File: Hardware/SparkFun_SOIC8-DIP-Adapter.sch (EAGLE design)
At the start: 15 parts, among them U1 GENERIC-SOIC8, U2 GENERIC-SOIC8, U3 GENERIC-SOIC8, U4 GENERIC-SOIC8

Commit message: Some small updates
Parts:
- FRAME1: value (none) -> frame
- JP1, JP2, JP3, JP4, JP5, JP6, JP7, JP8: value (none) -> 1x4
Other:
- note added: "Four SOIC8 to DIP adapters on one snappable board."
- note added: "V11"
- note removed: "V01"
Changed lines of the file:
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@@
 </classes>
 <parts>
-<part name="FRAME1" library="SparkFun-Aesthetics" deviceset="FRAME-LETTER" device=""/>
+<part name="FRAME1" library="SparkFun-Aesthetics" deviceset="FRAME-LETTER" device="" value="frame"/>
 <part name="U1" library="SparkFun-AnalogIC" deviceset="GENERIC-SOIC8" device=""/>
 <part name="U2" library="SparkFun-AnalogIC" deviceset="GENERIC-SOIC8" device=""/>
 <part name="U3" library="SparkFun-AnalogIC" deviceset="GENERIC-SOIC8" device=""/>
 <part name="U4" library="SparkFun-AnalogIC" deviceset="GENERIC-SOIC8" device=""/>
-<part name="JP1" library="SparkFun-Connectors" deviceset="M04" device="NO_SILK_ALL_ROUND"/>
-<part name="JP2" library="SparkFun-Connectors" deviceset="M04" device="NO_SILK_ALL_ROUND"/>
-<part name="JP3" library="SparkFun-Connectors" deviceset="M04" device="NO_SILK_ALL_ROUND"/>
-<part name="JP4" library="SparkFun-Connectors" deviceset="M04" device="NO_SILK_ALL_ROUND"/>
-<part name="JP5" library="SparkFun-Connectors" deviceset="M04" device="NO_SILK_ALL_ROUND"/>
-<part name="JP6" library="SparkFun-Connectors" deviceset="M04" device="NO_SILK_ALL_ROUND"/>
-<part name="JP7" library="SparkFun-Connectors" deviceset="M04" device="NO_SILK_ALL_ROUND"/>
-<part name="JP8" library="SparkFun-Connectors" deviceset="M04" device="NO_SILK_ALL_ROUND"/>
+<part name="JP1" library="SparkFun-Connectors" deviceset="M04" device="NO_SILK_ALL_ROUND" value="1x4"/>
+<part name="JP2" library="SparkFun-Connectors" deviceset="M04" device="NO_SILK_ALL_ROUND" value="1x4"/>
+<part name="JP3" library="SparkFun-Connectors" deviceset="M04" device="NO_SILK_ALL_ROUND" value="1x4"/>
+<part name="JP4" library="SparkFun-Connectors" deviceset="M04" device="NO_SILK_ALL_ROUND" value="1x4"/>
+<part name="JP5" library="SparkFun-Connectors" deviceset="M04" device="NO_SILK_ALL_ROUND" value="1x4"/>
+<part name="JP6" library="SparkFun-Connectors" deviceset="M04" device="NO_SILK_ALL_ROUND" value="1x4"/>
+<part name="JP7" library="SparkFun-Connectors" deviceset="M04" device="NO_SILK_ALL_ROUND" value="1x4"/>
+<part name="JP8" library="SparkFun-Connectors" deviceset="M04" device="NO_SILK_ALL_ROUND" value="1x4"/>
 <part name="LOGO1" library="SparkFun-Aesthetics" deviceset="SFE_LOGO_FLAME" device=".1_INCH"/>
 <part name="LOGO2" library="SparkFun-Aesthetics" deviceset="OSHW-LOGO" device="S"/>
@@
 <plain>
 <text x="172.72" y="10.16" size="2.54" layer="94">Byron Jacquot</text>
-<text x="238.76" y="7.62" size="2.54" layer="94">V01</text>
+<text x="238.76" y="7.62" size="2.54" layer="94">V11</text>
+<text x="68.58" y="172.72" size="2.54" layer="94">Four SOIC8 to DIP adapters on one snappable board.</text>
 </plain>
 <instances>

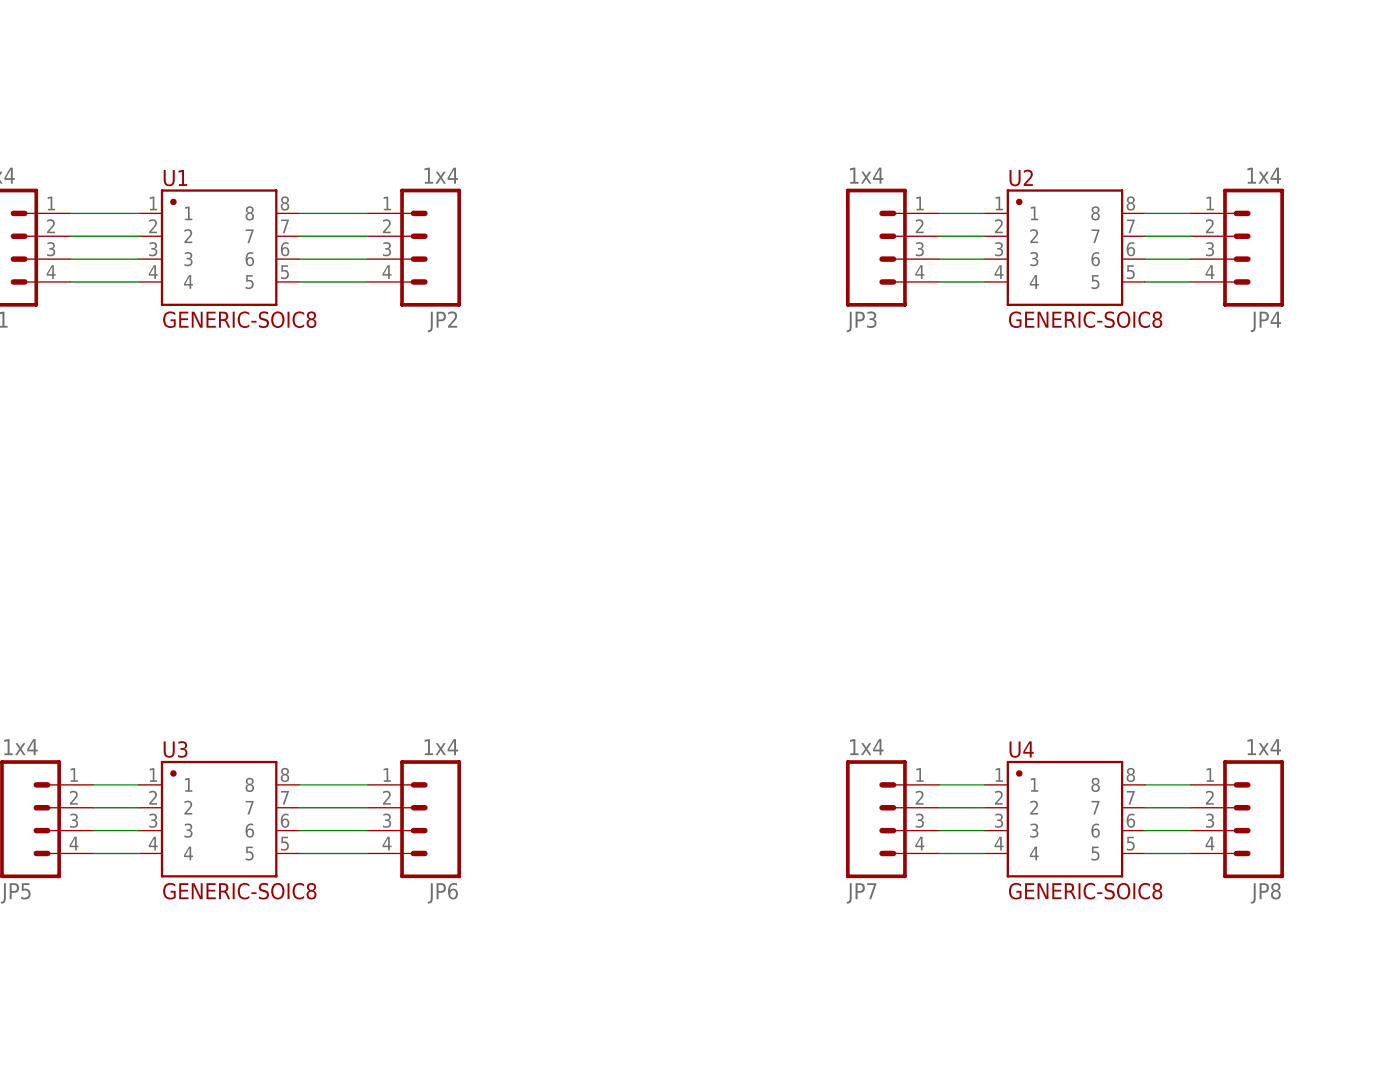
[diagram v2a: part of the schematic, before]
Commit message: Checklist-related updates.
Should handle all issues:
-names/values were on wring layers
-added dimension lines
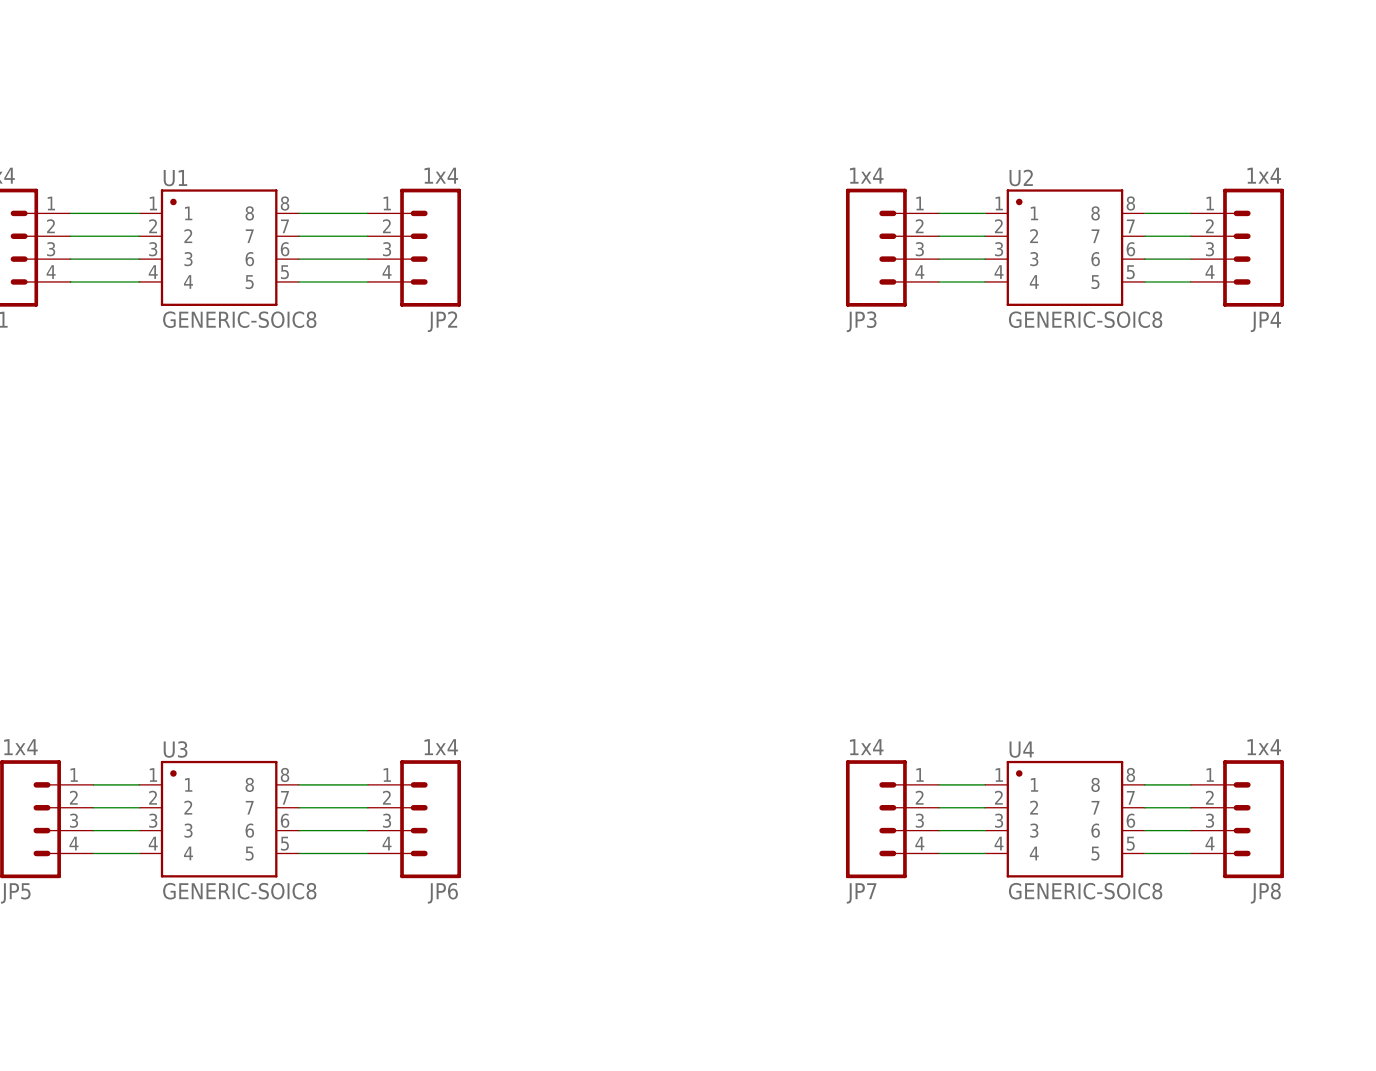
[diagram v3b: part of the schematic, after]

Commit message: Updates after reviewing protos.
Wider SOIC footprint.
DIP pin 1 marked with square pad.
Some rearrangement of silk elements.
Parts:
- JP1, JP3, JP5, JP7: device SparkFun-Connectors:M04NO_SILK_ALL_ROUND -> SparkFun-Connectors:M041X04_NO_SILK
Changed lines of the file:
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@@
 <part name="U3" library="SparkFun-AnalogIC" deviceset="GENERIC-SOIC8" device=""/>
 <part name="U4" library="SparkFun-AnalogIC" deviceset="GENERIC-SOIC8" device=""/>
-<part name="JP1" library="SparkFun-Connectors" deviceset="M04" device="NO_SILK_ALL_ROUND" value="1x4"/>
+<part name="JP1" library="SparkFun-Connectors" deviceset="M04" device="1X04_NO_SILK" value="1x4"/>
 <part name="JP2" library="SparkFun-Connectors" deviceset="M04" device="NO_SILK_ALL_ROUND" value="1x4"/>
-<part name="JP3" library="SparkFun-Connectors" deviceset="M04" device="NO_SILK_ALL_ROUND" value="1x4"/>
+<part name="JP3" library="SparkFun-Connectors" deviceset="M04" device="1X04_NO_SILK" value="1x4"/>
 <part name="JP4" library="SparkFun-Connectors" deviceset="M04" device="NO_SILK_ALL_ROUND" value="1x4"/>
-<part name="JP5" library="SparkFun-Connectors" deviceset="M04" device="NO_SILK_ALL_ROUND" value="1x4"/>
+<part name="JP5" library="SparkFun-Connectors" deviceset="M04" device="1X04_NO_SILK" value="1x4"/>
 <part name="JP6" library="SparkFun-Connectors" deviceset="M04" device="NO_SILK_ALL_ROUND" value="1x4"/>
-<part name="JP7" library="SparkFun-Connectors" deviceset="M04" device="NO_SILK_ALL_ROUND" value="1x4"/>
+<part name="JP7" library="SparkFun-Connectors" deviceset="M04" device="1X04_NO_SILK" value="1x4"/>
 <part name="JP8" library="SparkFun-Connectors" deviceset="M04" device="NO_SILK_ALL_ROUND" value="1x4"/>
 <part name="LOGO1" library="SparkFun-Aesthetics" deviceset="SFE_LOGO_FLAME" device=".1_INCH"/>

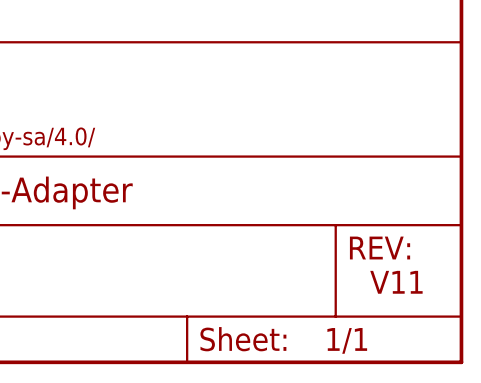
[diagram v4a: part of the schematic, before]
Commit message: Fixing review issues
* CC block location.
* Ver # mismatch between schem and PCB.
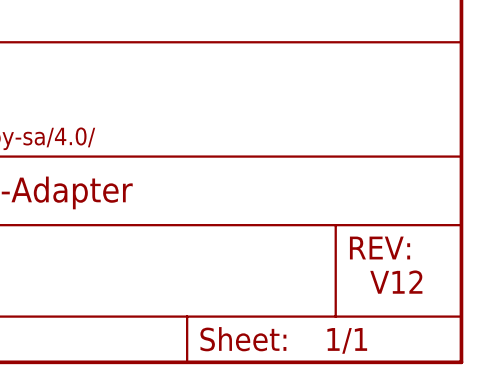
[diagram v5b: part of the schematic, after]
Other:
- note added: "V12"
- note removed: "V11"
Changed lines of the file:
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@@
 <plain>
 <text x="172.72" y="10.16" size="2.54" layer="94">Byron Jacquot</text>
-<text x="238.76" y="7.62" size="2.54" layer="94">V11</text>
+<text x="238.76" y="7.62" size="2.54" layer="94">V12</text>
 <text x="68.58" y="172.72" size="2.54" layer="94">Four SOIC8 to DIP adapters on one snappable board.</text>
 </plain>

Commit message: Moving version numbers back to V11, matching branch name.
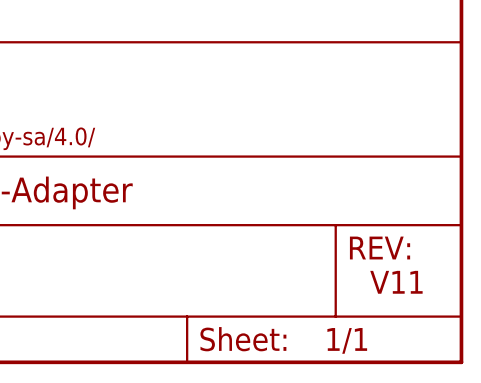
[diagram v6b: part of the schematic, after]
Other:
- note added: "V11"
- note removed: "V12"
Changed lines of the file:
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@@
 <?xml version="1.0" encoding="utf-8"?>
 <!DOCTYPE eagle SYSTEM "eagle.dtd">
-<eagle version="7.1.0">
+<eagle version="7.3.0">
 <drawing>
 <settings>
@@
 <plain>
 <text x="172.72" y="10.16" size="2.54" layer="94">Byron Jacquot</text>
-<text x="238.76" y="7.62" size="2.54" layer="94">V12</text>
+<text x="238.76" y="7.62" size="2.54" layer="94">V11</text>
 <text x="68.58" y="172.72" size="2.54" layer="94">Four SOIC8 to DIP adapters on one snappable board.</text>
 </plain>
